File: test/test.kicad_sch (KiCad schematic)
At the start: 2 parts

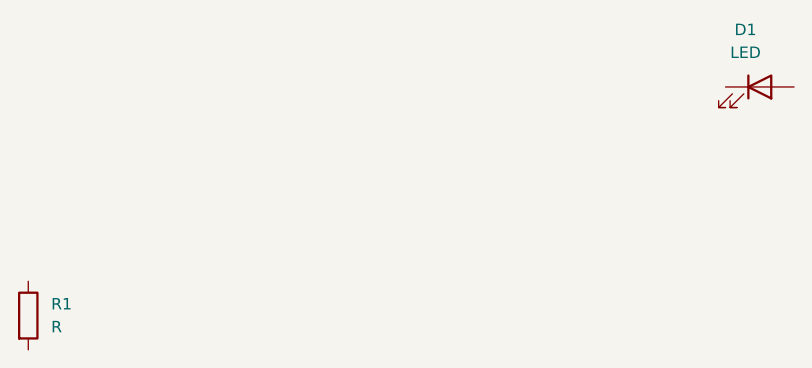
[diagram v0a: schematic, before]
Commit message: wire gemacht zwischen resistor und led + led nach unten verschoben
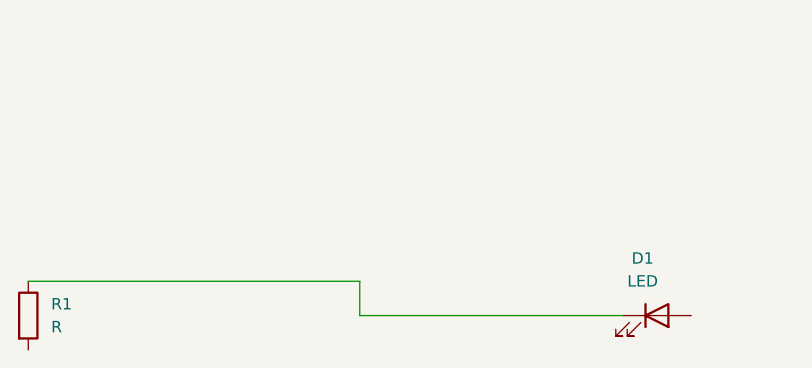
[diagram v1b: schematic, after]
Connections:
- net at R1.1: now also D1.1 (K)
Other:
- moved on the sheet: D1
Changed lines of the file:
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@@
 		(comment 1 "Kein kommentar 1")
+	)
+	(wire
+		(pts
+			(xy 130.81 101.6) (xy 160.02 101.6)
+		)
+		(stroke
+			(width 0)
+			(type default)
+		)
+	)
+	(wire
+		(pts
+			(xy 93.98 97.79) (xy 130.81 97.79)
+		)
+		(stroke
+			(width 0)
+			(type default)
+		)
+	)
+	(wire
+		(pts
+			(xy 130.81 97.79) (xy 130.81 101.6)
+		)
+		(stroke
+			(width 0)
+			(type default)
+		)
 	)
 	(symbol
@@
 	(symbol
 		(lib_id "Device:LED")
-		(at 175.26 76.2 0)
+		(at 163.83 101.6 0)
 		(unit 1)
 		(body_style 1)
@@
 		(fields_autoplaced yes)
 		(property "Reference" "D1"
-			(at 173.6725 69.85 0)
+			(at 162.2425 95.25 0)
 			(show_name no)
 			(do_not_autoplace no)
@@
 		)
 		(property "Value" "LED"
-			(at 173.6725 72.39 0)
+			(at 162.2425 97.79 0)
 			(show_name no)
 			(do_not_autoplace no)
@@
 		)
 		(property "Footprint" ""
-			(at 175.26 76.2 0)
+			(at 163.83 101.6 0)
 			(hide yes)
 			(show_name no)
@@
 		)
 		(property "Datasheet" ""
-			(at 175.26 76.2 0)
+			(at 163.83 101.6 0)
 			(hide yes)
 			(show_name no)
@@
 		)
 		(property "Description" "Light emitting diode"
-			(at 175.26 76.2 0)
+			(at 163.83 101.6 0)
 			(hide yes)
 			(show_name no)
@@
 		)
 		(property "Sim.Pins" "1=K 2=A"
-			(at 175.26 76.2 0)
+			(at 163.83 101.6 0)
 			(hide yes)
 			(show_name no)

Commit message: alles removed
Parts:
- removed D1: LED, symbol Device:LED
- removed R1: R, symbol Device:R
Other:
- company: SELAB Corps. -> (none)
- title: Das beste Schema -> (none)
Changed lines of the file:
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@@
 	(generator_version "10.0")
 	(paper "A4")
-	(title_block
-		(title "Das beste Schema")
-		(date "2026-06-07")
-		(rev "v1")
-		(company "SELAB Corps.")
-		(comment 1 "Kein kommentar 1")
-	)
-	(wire
-		(pts
-			(xy 130.81 101.6) (xy 160.02 101.6)
-		)
-		(stroke
-			(width 0)
-			(type default)
-		)
-	)
-	(wire
-		(pts
-			(xy 93.98 97.79) (xy 130.81 97.79)
-		)
-		(stroke
-			(width 0)
-			(type default)
-		)
-	)
-	(wire
-		(pts
-			(xy 130.81 97.79) (xy 130.81 101.6)
-		)
-		(stroke
-			(width 0)
-			(type default)
-		)
-	)
-	(symbol
-		(lib_id "Device:R")
-		(at 93.98 101.6 0)
-		(unit 1)
-		(body_style 1)
-		(exclude_from_sim no)
-		(in_bom yes)
-		(on_board yes)
-		(in_pos_files yes)
-		(dnp no)
-		(fields_autoplaced yes)
-		(property "Reference" "R1"
-			(at 96.52 100.3299 0)
-			(show_name no)
-			(do_not_autoplace no)
-			(effects
-				(font
-					(size 1.27 1.27)
-				)
-				(justify left)
-			)
-		)
-		(property "Value" "R"
-			(at 96.52 102.8699 0)
-			(show_name no)
-			(do_not_autoplace no)
-			(effects
-				(font
-					(size 1.27 1.27)
-				)
-				(justify left)
-			)
-		)
-		(property "Footprint" ""
-			(at 92.202 101.6 90)
-			(hide yes)
-			(show_name no)
-			(do_not_autoplace no)
-			(effects
-				(font
-					(size 1.27 1.27)
-				)
-			)
-		)
-		(property "Datasheet" ""
-			(at 93.98 101.6 0)
-			(hide yes)
-			(show_name no)
-			(do_not_autoplace no)
-			(effects
-				(font
-					(size 1.27 1.27)
-				)
-			)
-		)
-		(property "Description" "Resistor"
-			(at 93.98 101.6 0)
-			(hide yes)
-			(show_name no)
-			(do_not_autoplace no)
-			(effects
-				(font
-					(size 1.27 1.27)
-				)
-			)
-		)
-		(pin "2"
-		)
-		(pin "1"
-		)
-		(instances
-			(project "test"
-				(path "/d188607b-07b7-4bdd-b2bb-7815ace5362f"
-					(reference "R1")
-					(unit 1)
-				)
-			)
-		)
-	)
-	(symbol
-		(lib_id "Device:LED")
-		(at 163.83 101.6 0)
-		(unit 1)
-		(body_style 1)
-		(exclude_from_sim no)
-		(in_bom yes)
-		(on_board yes)
-		(in_pos_files yes)
-		(dnp no)
-		(fields_autoplaced yes)
-		(property "Reference" "D1"
-			(at 162.2425 95.25 0)
-			(show_name no)
-			(do_not_autoplace no)
-			(effects
-				(font
-					(size 1.27 1.27)
-				)
-			)
-		)
-		(property "Value" "LED"
-			(at 162.2425 97.79 0)
-			(show_name no)
-			(do_not_autoplace no)
-			(effects
-				(font
-					(size 1.27 1.27)
-				)
-			)
-		)
-		(property "Footprint" ""
-			(at 163.83 101.6 0)
-			(hide yes)
-			(show_name no)
-			(do_not_autoplace no)
-			(effects
-				(font
-					(size 1.27 1.27)
-				)
-			)
-		)
-		(property "Datasheet" ""
-			(at 163.83 101.6 0)
-			(hide yes)
-			(show_name no)
-			(do_not_autoplace no)
-			(effects
-				(font
-					(size 1.27 1.27)
-				)
-			)
-		)
-		(property "Description" "Light emitting diode"
-			(at 163.83 101.6 0)
-			(hide yes)
-			(show_name no)
-			(do_not_autoplace no)
-			(effects
-				(font
-					(size 1.27 1.27)
-				)
-			)
-		)
-		(property "Sim.Pins" "1=K 2=A"
-			(at 163.83 101.6 0)
-			(hide yes)
-			(show_name no)
-			(do_not_autoplace no)
-			(effects
-				(font
-					(size 1.27 1.27)
-				)
-			)
-		)
-		(pin "1"
-		)
-		(pin "2"
-		)
-		(instances
-			(project "test"
-				(path "/d188607b-07b7-4bdd-b2bb-7815ace5362f"
-					(reference "D1")
-					(unit 1)
-				)
-			)
-		)
-	)
 	(sheet_instances
 		(path "/"

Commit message: +led + resistor + wire
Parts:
- added D1: LED, symbol Device:LED
- added R1: R, symbol Device:R
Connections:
- new net: D1.1 (K), R1.1
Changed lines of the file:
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@@
 	(generator_version "10.0")
 	(paper "A4")
+	(wire
+		(pts
+			(xy 96.52 114.3) (xy 101.6 114.3)
+		)
+		(stroke
+			(width 0)
+			(type default)
+		)
+	)
+	(wire
+		(pts
+			(xy 96.52 110.49) (xy 96.52 114.3)
+		)
+		(stroke
+			(width 0)
+			(type default)
+		)
+	)
+	(wire
+		(pts
+			(xy 54.61 110.49) (xy 96.52 110.49)
+		)
+		(stroke
+			(width 0)
+			(type default)
+		)
+	)
+	(symbol
+		(lib_id "Device:LED")
+		(at 105.41 114.3 0)
+		(unit 1)
+		(body_style 1)
+		(exclude_from_sim no)
+		(in_bom yes)
+		(on_board yes)
+		(in_pos_files yes)
+		(dnp no)
+		(fields_autoplaced yes)
+		(property "Reference" "D1"
+			(at 103.8225 107.95 0)
+			(show_name no)
+			(do_not_autoplace no)
+			(effects
+				(font
+					(size 1.27 1.27)
+				)
+			)
+		)
+		(property "Value" "LED"
+			(at 103.8225 110.49 0)
+			(show_name no)
+			(do_not_autoplace no)
+			(effects
+				(font
+					(size 1.27 1.27)
+				)
+			)
+		)
+		(property "Footprint" ""
+			(at 105.41 114.3 0)
+			(hide yes)
+			(show_name no)
+			(do_not_autoplace no)
+			(effects
+				(font
+					(size 1.27 1.27)
+				)
+			)
+		)
+		(property "Datasheet" ""
+			(at 105.41 114.3 0)
+			(hide yes)
+			(show_name no)
+			(do_not_autoplace no)
+			(effects
+				(font
+					(size 1.27 1.27)
+				)
+			)
+		)
+		(property "Description" "Light emitting diode"
+			(at 105.41 114.3 0)
+			(hide yes)
+			(show_name no)
+			(do_not_autoplace no)
+			(effects
+				(font
+					(size 1.27 1.27)
+				)
+			)
+		)
+		(property "Sim.Pins" "1=K 2=A"
+			(at 105.41 114.3 0)
+			(hide yes)
+			(show_name no)
+			(do_not_autoplace no)
+			(effects
+				(font
+					(size 1.27 1.27)
+				)
+			)
+		)
+		(pin "1"
+		)
+		(pin "2"
+		)
+		(instances
+			(project "test"
+				(path "/d188607b-07b7-4bdd-b2bb-7815ace5362f"
+					(reference "D1")
+					(unit 1)
+				)
+			)
+		)
+	)
+	(symbol
+		(lib_id "Device:R")
+		(at 54.61 114.3 0)
+		(unit 1)
+		(body_style 1)
+		(exclude_from_sim no)
+		(in_bom yes)
+		(on_board yes)
+		(in_pos_files yes)
+		(dnp no)
+		(fields_autoplaced yes)
+		(property "Reference" "R1"
+			(at 57.15 113.0299 0)
+			(show_name no)
+			(do_not_autoplace no)
+			(effects
+				(font
+					(size 1.27 1.27)
+				)
+				(justify left)
+			)
+		)
+		(property "Value" "R"
+			(at 57.15 115.5699 0)
+			(show_name no)
+			(do_not_autoplace no)
+			(effects
+				(font
+					(size 1.27 1.27)
+				)
+				(justify left)
+			)
+		)
+		(property "Footprint" ""
+			(at 52.832 114.3 90)
+			(hide yes)
+			(show_name no)
+			(do_not_autoplace no)
+			(effects
+				(font
+					(size 1.27 1.27)
+				)
+			)
+		)
+		(property "Datasheet" ""
+			(at 54.61 114.3 0)
+			(hide yes)
+			(show_name no)
+			(do_not_autoplace no)
+			(effects
+				(font
+					(size 1.27 1.27)
+				)
+			)
+		)
+		(property "Description" "Resistor"
+			(at 54.61 114.3 0)
+			(hide yes)
+			(show_name no)
+			(do_not_autoplace no)
+			(effects
+				(font
+					(size 1.27 1.27)
+				)
+			)
+		)
+		(pin "1"
+		)
+		(pin "2"
+		)
+		(instances
+			(project "test"
+				(path "/d188607b-07b7-4bdd-b2bb-7815ace5362f"
+					(reference "R1")
+					(unit 1)
+				)
+			)
+		)
+	)
 	(sheet_instances
 		(path "/"

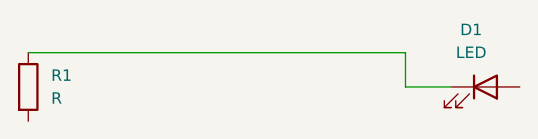
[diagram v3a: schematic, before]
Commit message: value und ref von led geändert + ref von resistor
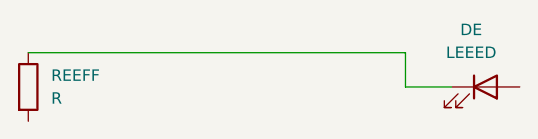
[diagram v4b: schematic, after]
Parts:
- DE: renamed from D1; value LED -> LEEED
- renumbered R1 to REEFF
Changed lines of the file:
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@@
 		(dnp no)
 		(fields_autoplaced yes)
-		(property "Reference" "D1"
+		(property "Reference" "DE"
 			(at 103.8225 107.95 0)
 			(show_name no)
@@
 			)
 		)
-		(property "Value" "LED"
+		(property "Value" "LEEED"
 			(at 103.8225 110.49 0)
 			(show_name no)
@@
 			(project "test"
 				(path "/d188607b-07b7-4bdd-b2bb-7815ace5362f"
-					(reference "D1")
+					(reference "DE")
 					(unit 1)
 				)
@@
 		(dnp no)
 		(fields_autoplaced yes)
-		(property "Reference" "R1"
+		(property "Reference" "REEFF"
 			(at 57.15 113.0299 0)
 			(show_name no)
@@
 			(project "test"
 				(path "/d188607b-07b7-4bdd-b2bb-7815ace5362f"
-					(reference "R1")
+					(reference "REEFF")
 					(unit 1)
 				)

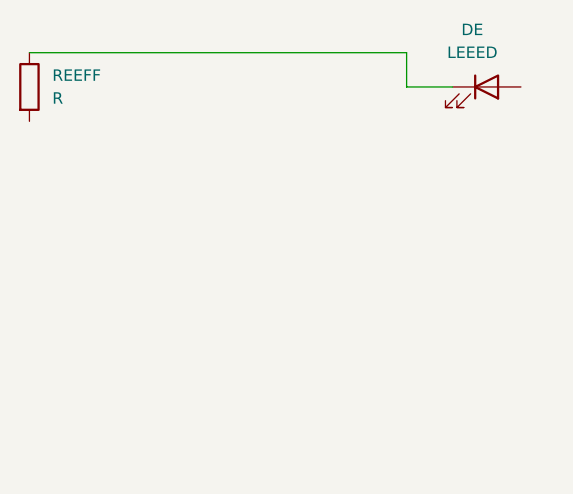
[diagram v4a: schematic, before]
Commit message: langes verschachteltes wire hinzugefügt und ein alten teil enfernt
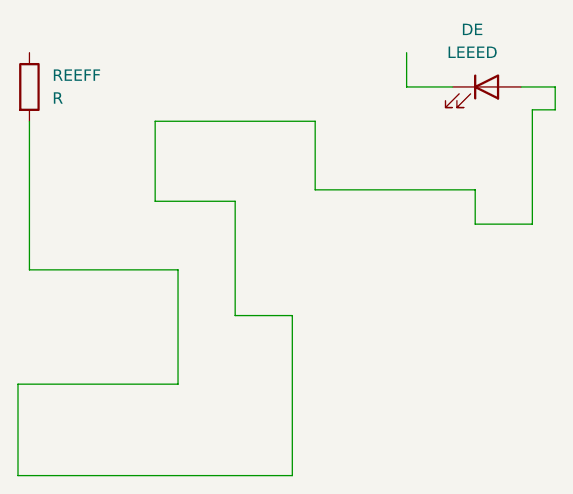
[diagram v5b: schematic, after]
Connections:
- net at DE.1 (K): no longer REEFF.1
- net at DE.2 (A): now also REEFF.2
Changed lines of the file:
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@@
+	(wire
+		(pts
+			(xy 86.36 118.11) (xy 86.36 125.73)
+		)
+		(stroke
+			(width 0)
+			(type default)
+		)
+	)
+	(wire
+		(pts
+			(xy 104.14 125.73) (xy 104.14 129.54)
+		)
+		(stroke
+			(width 0)
+			(type default)
+		)
+	)
+	(wire
+		(pts
+			(xy 71.12 147.32) (xy 53.34 147.32)
+		)
+		(stroke
+			(width 0)
+			(type default)
+		)
+	)
+	(wire
+		(pts
+			(xy 77.47 127) (xy 68.58 127)
+		)
+		(stroke
+			(width 0)
+			(type default)
+		)
+	)
+	(wire
+		(pts
+			(xy 110.49 116.84) (xy 113.03 116.84)
+		)
+		(stroke
+			(width 0)
+			(type default)
+		)
+	)
+	(wire
+		(pts
+			(xy 104.14 129.54) (xy 110.49 129.54)
+		)
+		(stroke
+			(width 0)
+			(type default)
+		)
+	)
+	(wire
+		(pts
+			(xy 83.82 139.7) (xy 77.47 139.7)
+		)
+		(stroke
+			(width 0)
+			(type default)
+		)
+	)
+	(wire
+		(pts
+			(xy 110.49 116.84) (xy 110.49 129.54)
+		)
+		(stroke
+			(width 0)
+			(type default)
+		)
+	)
+	(wire
+		(pts
+			(xy 86.36 125.73) (xy 104.14 125.73)
+		)
+		(stroke
+			(width 0)
+			(type default)
+		)
+	)
+	(wire
+		(pts
+			(xy 68.58 127) (xy 68.58 118.11)
+		)
+		(stroke
+			(width 0)
+			(type default)
+		)
+	)
 	(wire
 		(pts
 			(xy 96.52 114.3) (xy 101.6 114.3)
+		)
+		(stroke
+			(width 0)
+			(type default)
+		)
+	)
+	(wire
+		(pts
+			(xy 77.47 139.7) (xy 77.47 127)
 		)
 		(stroke
@@
 	(wire
 		(pts
-			(xy 54.61 110.49) (xy 96.52 110.49)
+			(xy 54.61 134.62) (xy 71.12 134.62)
 		)
 		(stroke
+			(width 0)
+			(type default)
+		)
+	)
+	(wire
+		(pts
+			(xy 54.61 118.11) (xy 54.61 134.62)
+		)
+		(stroke
+			(width 0)
+			(type default)
+		)
+	)
+	(wire
+		(pts
+			(xy 113.03 114.3) (xy 109.22 114.3)
+		)
+		(stroke
+			(width 0)
+			(type default)
+		)
+	)
+	(wire
+		(pts
+			(xy 113.03 116.84) (xy 113.03 114.3)
+		)
+		(stroke
+			(width 0)
+			(type default)
+		)
+	)
+	(wire
+		(pts
+			(xy 71.12 134.62) (xy 71.12 147.32)
+		)
+		(stroke
+			(width 0)
+			(type default)
+		)
+	)
+	(wire
+		(pts
+			(xy 53.34 157.48) (xy 83.82 157.48)
+		)
+		(stroke
+			(width 0)
+			(type default)
+		)
+	)
+	(wire
+		(pts
+			(xy 83.82 157.48) (xy 83.82 139.7)
+		)
+		(stroke
+			(width 0)
+			(type default)
+		)
+	)
+	(wire
+		(pts
+			(xy 68.58 118.11) (xy 86.36 118.11)
+		)
+		(stroke
+			(width 0)
+			(type default)
+		)
+	)
+	(wire
+		(pts
+			(xy 53.34 147.32) (xy 53.34 157.48)
+		)
+		(stroke

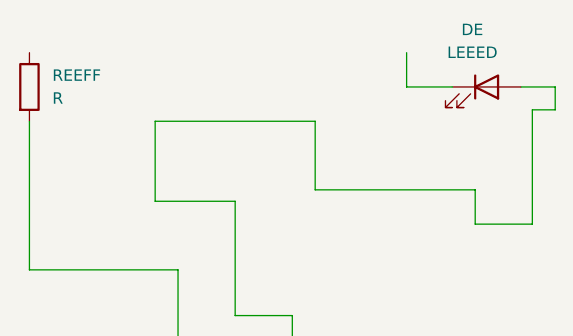
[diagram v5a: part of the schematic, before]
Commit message: added wire to make circle
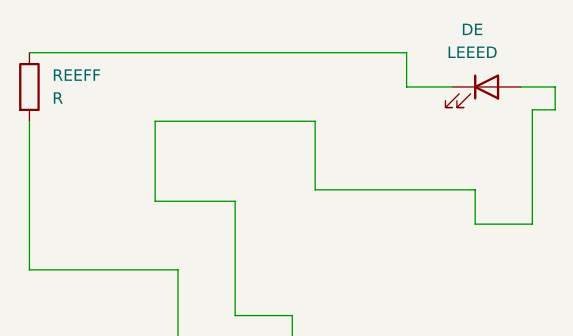
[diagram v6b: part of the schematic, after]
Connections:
- net at DE.1 (K): now also REEFF.1
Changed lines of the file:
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@@
+	(wire
+		(pts
+			(xy 54.61 110.49) (xy 96.52 110.49)
+		)
+		(stroke
+			(width 0)
+			(type default)
+		)
+	)
 	(wire
 		(pts

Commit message: Titel + Date added
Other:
- title: (none) -> Titelll !
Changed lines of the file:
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@@
 	(generator_version "10.0")
 	(paper "A4")
+	(title_block
+		(title "Titelll !")
+		(date "2026-06-23")
+	)
 	(wire
 		(pts

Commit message: added every info to title
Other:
- company: (none) -> firma 
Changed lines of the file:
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@@
 		(title "Titelll !")
 		(date "2026-06-23")
+		(rev "REv +1")
+		(company "firma ")
+		(comment 1 "comment 1")
+		(comment 2 "comment 2")
+		(comment 3 "comment 3")
+		(comment 4 "comment 4")
+		(comment 5 "comment 5")
+		(comment 6 "comment 6")
+		(comment 7 "comment 7")
+		(comment 8 "comment 8")
+		(comment 9 "comment 9")
 	)
 	(wire
